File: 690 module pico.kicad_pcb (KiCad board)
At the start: 2 copper layers, 67.7 x 21 mm, 14 parts, among them J1 Conn_01x04_Male, J2 USB_B_Micro, SW1 Bootsel, SW2 Reset, U1 USBLC6-2P6, U2 DA14695_000HQ2

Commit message: Ordered version 1
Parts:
- added TP1: Vbat, TestPoint:TestPoint_Pad_1.0x1.0mm_custom, B.Cu at (103.5, 71.4)
- added TP2: Vbus, TestPoint:TestPoint_Pad_1.0x1.0mm_custom, B.Cu at (105.0, 71.4)
- added TP3: USB_P, TestPoint:TestPoint_Pad_1.0x1.0mm_custom, B.Cu at (111.1, 65.1)
- added TP4: USB_N, TestPoint:TestPoint_Pad_1.0x1.0mm_custom, B.Cu at (111.1, 68.6)
- added TP5: UART_TX, TestPoint:TestPoint_Pad_1.0x1.0mm_custom, B.Cu at (102.7, 63.0)
- added TP6: UART_RX, TestPoint:TestPoint_Pad_1.0x1.0mm_custom, B.Cu at (104.2, 63.0)
- added TP7: ~{Bootsel}, TestPoint:TestPoint_Pad_1.0x1.0mm_custom, B.Cu at (98.4, 65.6)
- added TP8: ~{RST}, TestPoint:TestPoint_Pad_1.0x1.0mm_custom, B.Cu at (98.4, 68.6)
- added TP9: GND, TestPoint:TestPoint_Pad_1.0x1.0mm_custom, B.Cu at (98.4, 67.1)
- moved R3 3.27 mm to (95.1, 70.7)
- moved SW2 3.27 mm to (99.7, 70.7)
- moved BT1 1.57 mm to (86.3, 70.7)
- moved REF** 1.52 mm to (104.0, 67.2)
- moved R2 1.21 mm to (94.9, 63.8)
- moved SW1 1.21 mm to (99.8, 63.8)
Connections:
- net /RST renamed /~{RST}
- net /bootsel renamed /~{Bootsel}
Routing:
- net VBUS: track 74.8 -> 79.3 mm
- net GND: track 42.8 -> 47.0 mm, vias 67 -> 78
- net +BATT: track 61.6 -> 65.2 mm
- net /USB_P: track 53.6 -> 57.1 mm
- net /UART_RX: track 72.2 -> 75.2 mm
- net /~{Bootsel}: track 47.8 -> 50.7 mm, vias 2 -> 3
- net /USB_N: track 52.7 -> 54.6 mm, vias 0 -> 1
- net /UART_TX: track 83.1 -> 85.0 mm
- net +3V0: track 68.1 -> 69.5 mm, vias 5 -> 4
- net /USR_LED: track 55.6 -> 54.3 mm
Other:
- board text added: "DA14695MOD Pico"
- board text added: "V1.0"
- board text removed: "DA14695 module Pico"

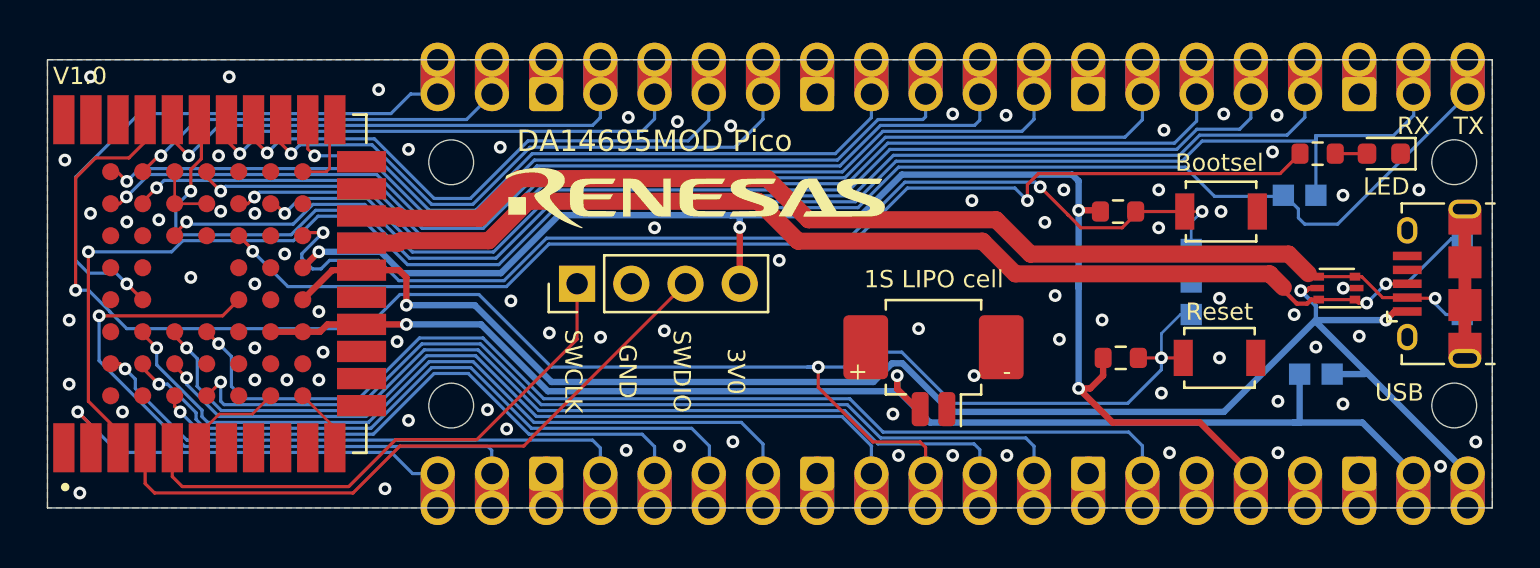
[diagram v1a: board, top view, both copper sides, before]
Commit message: Added pinout picture
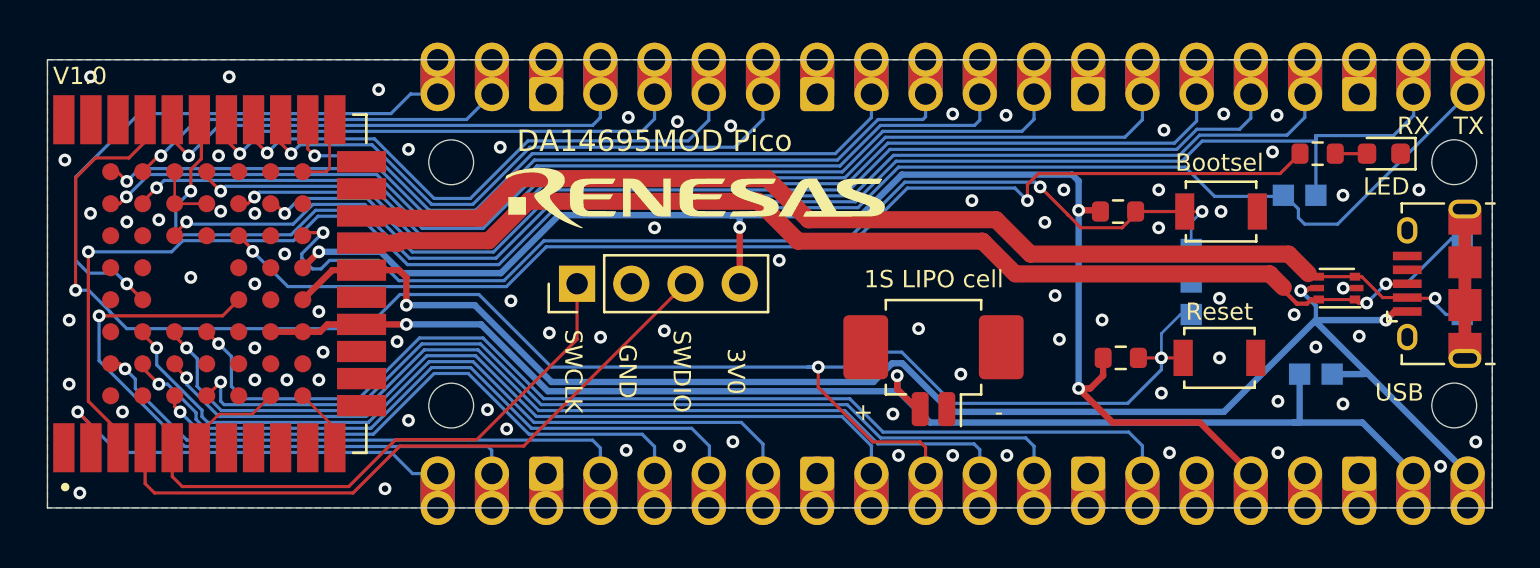
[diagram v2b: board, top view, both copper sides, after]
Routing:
- net +3V0: track 69.5 -> 68.7 mm
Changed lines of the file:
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@@
     )
     (pad_to_mask_clearance 0)
-    (solder_mask_min_width 0.12)
     (grid_origin 111.33 56.7)
     (pcbplotparams
-      (layerselection 0x00010fc_ffffffff)
+      (layerselection 0x0000008_7ffffffe)
       (disableapertmacros false)
-      (usegerberextensions false)
-      (usegerberattributes true)
-      (usegerberadvancedattributes true)
-      (creategerberjobfile true)
+      (usegerberextensions true)
+      (usegerberattributes false)
+      (usegerberadvancedattributes false)
+      (creategerberjobfile false)
       (svguseinch false)
       (svgprecision 6)
@@
       (psa4output false)
       (plotreference true)
-      (plotvalue true)
+      (plotvalue false)
       (plotinvisibletext false)
       (sketchpadsonfab false)
-      (subtractmaskfromsilk false)
+      (subtractmaskfromsilk true)
       (outputformat 1)
       (mirror false)
-      (drillshape 1)
+      (drillshape 0)
       (scaleselection 1)
-      (outputdirectory "")
+      (outputdirectory "./")
     )
   )
@@
     (pad "2" smd roundrect (at 0.625 -2.4 180) (size 0.8 1.6) (layers "F.Cu" "F.Paste" "F.Mask") (roundrect_rratio 0.25)
       (net 16 "+BATT") (pinfunction "+") (pintype "passive"))
-    (pad "MP" smd roundrect (at -3.175 0.5 180) (size 2.1 3) (layers "F.Cu" "F.Paste" "F.Mask") (roundrect_rratio 0.119048))
-    (pad "MP" smd roundrect (at 3.175 0.5 180) (size 2.1 3) (layers "F.Cu" "F.Paste" "F.Mask") (roundrect_rratio 0.119048))
+    (pad "MP" smd roundrect (at -3.175 0.5 180) (size 2.1 3) (layers "F.Cu" "F.Paste" "F.Mask") (roundrect_rratio 0.1190480952))
+    (pad "MP" smd roundrect (at 3.175 0.5 180) (size 2.1 3) (layers "F.Cu" "F.Paste" "F.Mask") (roundrect_rratio 0.1190480952))
     (model "${KICAD6_3DMODEL_DIR}/Connector_Molex.3dshapes/Molex_PicoBlade_53261-0271_1x02-1MP_P1.25mm_Horizontal.wrl"
       (offset (xyz 0 0 0))
@@
     (property "Sheetfile" "690 module pico.kicad_sch")
     (property "Sheetname" "")
-    (attr through_hole)
+    (attr smd)
     (fp_text reference "U2" (at -4.823 -13.781 90) (layer "F.SilkS") hide
       (effects (font (size 1 1) (thickness 0.15)))
@@
     (effects (font (size 0.8128 0.8128) (thickness 0.1524)))
   )
-  (gr_text "-" (at 89.74 71.305) (layer "F.SilkS")
+  (gr_text "-" (at 89.359 73.21) (layer "F.SilkS")
     (effects (font (size 0.8128 0.8128) (thickness 0.1524)))
   )
@@
     (effects (font (size 0.8128 0.8128) (thickness 0.1524)))
   )
-  (gr_text "+" (at 82.755 71.305) (layer "F.SilkS")
+  (gr_text "+" (at 83.009 73.21) (layer "F.SilkS")
     (effects (font (size 0.8128 0.8128) (thickness 0.1524)))
   )
@@
   (via (at 88.1 63.3) (size 0.6) (drill 0.3) (layers "F.Cu" "B.Cu") (free) (net 1))
   (via (at 68.3 69.5) (size 0.6) (drill 0.3) (layers "F.Cu" "B.Cu") (free) (net 1))
-  (via (at 88.2 71.5) (size 0.6) (drill 0.3) (layers "F.Cu" "B.Cu") (free) (net 1))
+  (via (at 87.581 71.432) (size 0.6) (drill 0.3) (layers "F.Cu" "B.Cu") (free) (net 1))
   (via (at 105.488 63.05) (size 0.6) (drill 0.3) (layers "F.Cu" "B.Cu") (free) (net 1))
   (via (at 103.201125 68.641599) (size 0.6) (drill 0.3) (layers "F.Cu" "B.Cu") (free) (net 1))
@@
   (segment (start 93.1 63.754) (end 94.064 63.754) (width 0.3) (layer "F.Cu") (net 3))
   (segment (start 56.744 66.445) (end 56.755 66.445) (width 0.3) (layer "F.Cu") (net 3))
-  (segment (start 93.1 63.881) (end 93.1 63.754) (width 0.3) (layer "F.Cu") (net 3))
   (via (at 93.1 63.754) (size 0.6) (drill 0.3) (layers "F.Cu" "B.Cu") (net 3))
   (via (at 77.22 64.5575) (size 0.6) (drill 0.3) (layers "F.Cu" "B.Cu") (net 3))
@@
   (via (at 57.5 65.7) (size 0.6) (drill 0.3) (layers "F.Cu" "B.Cu") (net 3))
   (segment (start 93.1 62.383) (end 92.8 62.083) (width 0.3) (layer "B.Cu") (net 3))
-  (segment (start 93.1 66.7) (end 93.1 67.4) (width 0.3) (layer "B.Cu") (net 3))
-  (segment (start 93.1 63.881) (end 93.1 66.7) (width 0.3) (layer "B.Cu") (net 3))
   (segment (start 60.4 65.7) (end 61.4 66.7) (width 0.3) (layer "B.Cu") (net 3))
   (segment (start 77.22 64.5575) (end 77.22 63.992) (width 0.3) (layer "B.Cu") (net 3))
@@
   (segment (start 93.1 63.881) (end 93.1 62.383) (width 0.3) (layer "B.Cu") (net 3))
   (segment (start 84.817 62.083) (end 82.917 63.983) (width 0.3) (layer "B.Cu") (net 3))
-  (segment (start 93.1 66.7) (end 93.1 72.1) (width 0.3) (layer "B.Cu") (net 3))
+  (segment (start 93.1 63.881) (end 93.1 72.1) (width 0.3) (layer "B.Cu") (net 3))
   (segment (start 98.63 77.7) (end 98.63 76.09) (width 1.6) (layer "F.Cu") (net 14))
   (segment (start 98.63 77.7) (end 98.63 76.09) (width 1.6) (layer "B.Cu") (net 14))
@@
   (via (at 54.4 65.6785) (size 0.6) (drill 0.3) (layers "F.Cu" "B.Cu") (net 47))
   (via (at 90.7 63.3) (size 0.6) (drill 0.3) (layers "F.Cu" "B.Cu") (net 47))
-  (segment (start 82.453541 65.336) (end 85.077541 62.712) (width 0.15) (layer "B.Cu") (net 47))
-  (segment (start 54.4 65.6785) (end 56.0505 67.329) (width 0.15) (layer "B.Cu") (net 47))
-  (segment (start 90.112 62.712) (end 90.7 63.3) (width 0.15) (layer "B.Cu") (net 47))
-  (segment (start 85.077541 62.712) (end 90.112 62.712) (width 0.15) (layer "B.Cu") (net 47))
-  (segment (start 68.282344 65.336) (end 82.453541 65.336) (width 0.15) (layer "B.Cu") (net 47))
-  (segment (start 66.289344 67.329) (end 68.282344 65.336) (width 0.15) (layer "B.Cu") (net 47))
   (segment (start 56.0505 67.329) (end 66.289344 67.329) (width 0.15) (layer "B.Cu") (net 47))
+  (segment (start 82.326541 65.463) (end 85.077541 62.712) (width 0.15) (layer "B.Cu") (net 47))
+  (segment (start 68.155344 65.463) (end 82.326541 65.463) (width 0.15) (layer "B.Cu") (net 47))
+  (segment (start 66.289344 67.329) (end 68.155344 65.463) (width 0.15) (layer "B.Cu") (net 47))
+  (segment (start 85.077541 62.712) (end 90.112 62.712) (width 0.15) (layer "B.Cu") (net 47))
+  (segment (start 90.112 62.712) (end 90.7 63.3) (width 0.15) (layer "B.Cu") (net 47))
+  (segment (start 54.4 65.6785) (end 56.0505 67.329) (width 0.15) (layer "B.Cu") (net 47))
   (segment (start 89.239 64.2) (end 90.845 65.806) (width 0.8) (layer "F.Cu") (net 49))
   (segment (start 59.5 64.02) (end 61.225001 64.02) (width 0.8) (layer "F.Cu") (net 49))
@@
   (via (at 57.7 64.8) (size 0.6) (drill 0.3) (layers "F.Cu" "B.Cu") (net 52))
   (via (at 98.884 63.812) (size 0.6) (drill 0.3) (layers "F.Cu" "B.Cu") (net 52))
-  (segment (start 57.6 66.5) (end 57.2 66.5) (width 0.15) (layer "B.Cu") (net 52))
-  (segment (start 82.338804 65.059) (end 68.167607 65.059) (width 0.15) (layer "B.Cu") (net 52))
+  (segment (start 68.040607 65.186) (end 66.174607 67.052) (width 0.15) (layer "B.Cu") (net 52))
+  (segment (start 91.0755 62.435) (end 84.962804 62.435) (width 0.15) (layer "B.Cu") (net 52))
+  (segment (start 84.962804 62.435) (end 82.211804 65.186) (width 0.15) (layer "B.Cu") (net 52))
+  (segment (start 56.7 65.790064) (end 57.690064 64.8) (width 0.15) (layer "B.Cu") (net 52))
+  (segment (start 66.174607 67.052) (end 61.252 67.052) (width 0.15) (layer "B.Cu") (net 52))
   (segment (start 56.7 66) (end 56.7 65.790064) (width 0.15) (layer "B.Cu") (net 52))
-  (segment (start 57.2 66.5) (end 56.7 66) (width 0.15) (layer "B.Cu") (net 52))
-  (segment (start 98.376 64.32) (end 98.884 63.812) (width 0.127) (layer "B.Cu") (net 52))
-  (segment (start 91.3 62.6595) (end 91.0755 62.435) (width 0.15) (layer "B.Cu") (net 52))
-  (segment (start 68.167607 65.059) (end 66.174607 67.052) (width 0.15) (layer "B.Cu") (net 52))
   (segment (start 58 66.1) (end 57.6 66.5) (width 0.15) (layer "B.Cu") (net 52))
   (segment (start 61.252 67.052) (end 60.3 66.1) (width 0.15) (layer "B.Cu") (net 52))
-  (segment (start 91.0755 62.435) (end 84.962804 62.435) (width 0.15) (layer "B.Cu") (net 52))
-  (segment (start 60.3 66.1) (end 58 66.1) (width 0.15) (layer "B.Cu") (net 52))
+  (segment (start 98.376 64.32) (end 98.884 63.812) (width 0.127) (layer "B.Cu") (net 52))
+  (segment (start 57.2 66.5) (end 56.7 66) (width 0.15) (layer "B.Cu") (net 52))
+  (segment (start 57.6 66.5) (end 57.2 66.5) (width 0.15) (layer "B.Cu") (net 52))
   (segment (start 98.376 65.59) (end 98.376 64.32) (width 0.127) (layer "B.Cu") (net 52))
+  (segment (start 91.3 62.6595) (end 91.0755 62.435) (width 0.15) (layer "B.Cu") (net 52))
+  (segment (start 82.211804 65.186) (end 68.040607 65.186) (width 0.15) (layer "B.Cu") (net 52))
+  (segment (start 60.3 66.1) (end 58 66.1) (width 0.15) (layer "B.Cu") (net 52))
   (segment (start 57.690064 64.8) (end 57.7 64.8) (width 0.15) (layer "B.Cu") (net 52))
-  (segment (start 56.7 65.790064) (end 57.690064 64.8) (width 0.15) (layer "B.Cu") (net 52))
-  (segment (start 66.174607 67.052) (end 61.252 67.052) (width 0.15) (layer "B.Cu") (net 52))
-  (segment (start 84.962804 62.435) (end 82.338804 65.059) (width 0.15) (layer "B.Cu") (net 52))
   (zone (net 1) (net_name "GND") (layers F&B.Cu) (hatch edge 0.508)
     (connect_pads (clearance 0.2))
